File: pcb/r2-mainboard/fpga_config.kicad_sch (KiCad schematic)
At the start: 32 parts, among them U700 XC6SLX-FTG256, U902 W25Q128JVSIQ, X900 33.33MHz

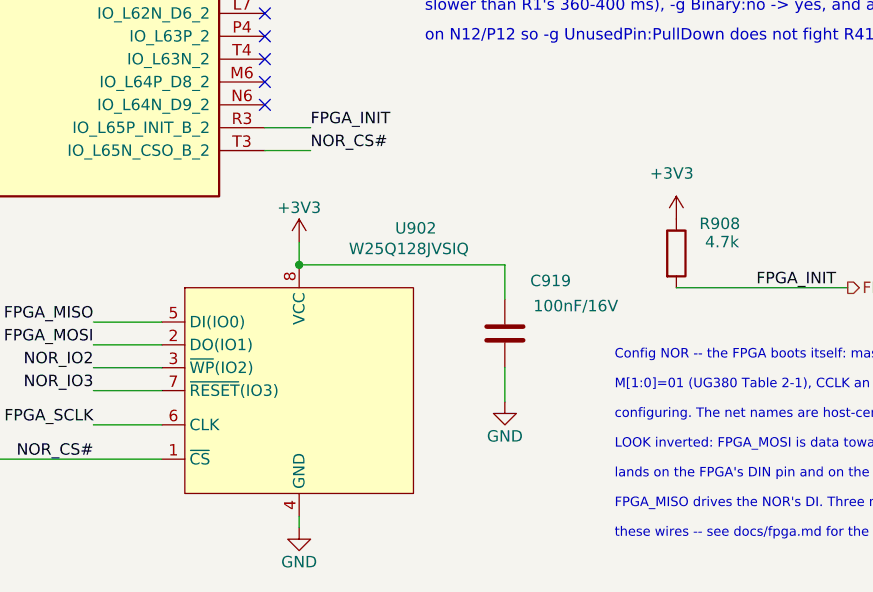
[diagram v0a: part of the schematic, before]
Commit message: changing to osb62x-pm
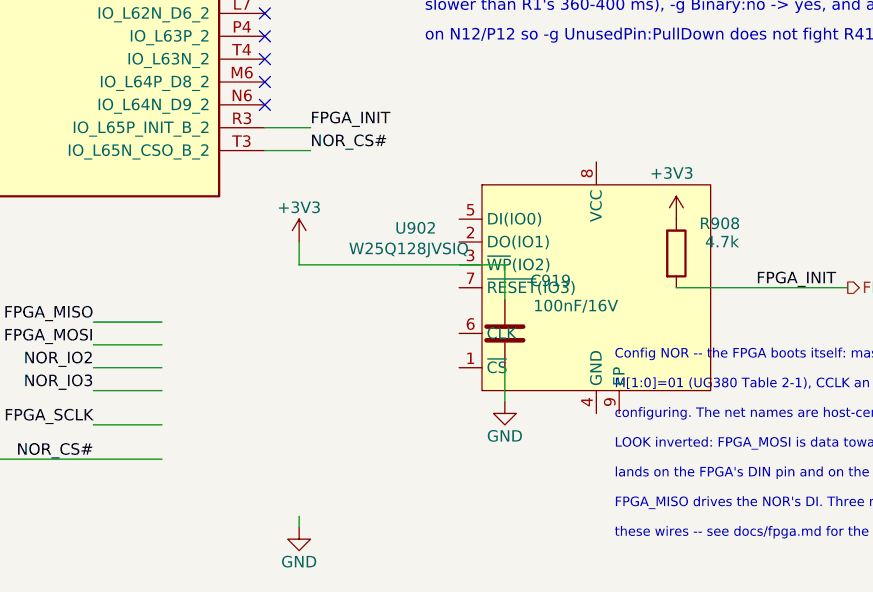
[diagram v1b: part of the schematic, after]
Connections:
- net +3V3: no longer U902.8 (VCC)
- net FPGA_MISO: no longer U902.5 (DI(IO0))
- net FPGA_MOSI: no longer U902.2 (DO(IO1))
- net FPGA_SCLK: no longer U902.6 (CLK)
- net GND: no longer U902.4 (GND)
- net NOR_CS#: no longer U902.1 (~{CS})
- net NOR_IO2: no longer U902.3 (~{WP}(IO2))
- net NOR_IO3: no longer U902.7 (~{RESET}(IO3))
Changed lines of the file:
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@@
 	)
 	(junction
-		(at 87.63 162.56)
-		(diameter 0)
-		(color 0 0 0 0)
-	)
-	(junction
 		(at 175.26 63.5)
 		(diameter 0)
@@
 			)
 		)
-		(property "Description" ""
+		(property "Description" "3.3V CMOS SMD Crystal Clock Oscillator, Abracon"
 			(at 233.68 55.88 0)
 			(hide yes)
@@
 			)
 		)
-		(property "Description" ""
+		(property "Description" "Unpolarized capacitor"
 			(at 208.28 85.09 0)
 			(hide yes)
@@
 			)
 		)
-		(property "Description" ""
+		(property "Description" "Resistor"
 			(at 185.42 35.56 0)
 			(hide yes)
@@
 			)
 		)
-		(property "Description" "NOR supply decoupling"
+		(property "Description" "Unpolarized capacitor"
 			(at 110.49 170.18 0)
 			(hide yes)
@@
 	)
 	(symbol
-		(lib_name "GND_1")
 		(lib_id "power:GND")
 		(at 175.26 71.12 0)
@@
 			)
 		)
-		(property "Description" ""
+		(property "Description" "Unpolarized capacitor"
 			(at 195.58 146.05 0)
 			(hide yes)
@@
 			)
 		)
-		(property "Description" ""
+		(property "Description" "Unpolarized capacitor"
 			(at 208.28 125.73 0)
 			(hide yes)
@@
 			)
 		)
-		(property "Description" ""
+		(property "Description" "Unpolarized capacitor"
 			(at 220.98 146.05 0)
 			(hide yes)
@@
 			)
 		)
-		(property "Description" ""
+		(property "Description" "Unpolarized capacitor"
 			(at 195.58 125.73 0)
 			(hide yes)
@@
 			)
 		)
-		(property "Description" ""
+		(property "Description" "Unpolarized capacitor"
 			(at 208.28 105.41 0)
 			(hide yes)
@@
 	)
 	(symbol
-		(lib_name "GND_1")
 		(lib_id "power:GND")
 		(at 233.68 109.22 0)
@@
 		(pin "8"
 		)
+		(pin "9"
+		)
 		(instances
 			(project "r2"
@@
 			)
 		)
-		(property "Description" ""
+		(property "Description" "Resistor"
 			(at 175.26 35.56 0)
 			(hide yes)
@@
 	)
 	(symbol
-		(lib_name "GND_1")
 		(lib_id "power:GND")
 		(at 233.68 149.86 0)
@@
 			)
 		)
-		(property "Description" ""
+		(property "Description" "Unpolarized capacitor"
 			(at 220.98 85.09 0)
 			(hide yes)
@@
 			)
 		)
-		(property "Description" ""
+		(property "Description" "Unpolarized capacitor"
 			(at 233.68 85.09 0)
 			(hide yes)
@@
 			)
 		)
-		(property "Description" ""
+		(property "Description" "Unpolarized capacitor"
 			(at 195.58 85.09 0)
 			(hide yes)
@@
 			)
 		)
-		(property "Description" ""
+		(property "Description" "Unpolarized capacitor"
 			(at 233.68 105.41 0)
 			(hide yes)
@@
 			)
 		)
-		(property "Description" "Series limit on the SoM's NOR chip select: the FPGA drives CSO_B during configuration, so the two briefly contend if software gets it wrong"
+		(property "Description" "Resistor"
 			(at 36.83 184.15 270)
 			(hide yes)
@@
 			)
 		)
-		(property "Description" ""
+		(property "Description" "Unpolarized capacitor"
 			(at 233.68 146.05 0)
 			(hide yes)
@@
 			)
 		)
-		(property "Description" ""
+		(property "Description" "Unpolarized capacitor"
 			(at 208.28 146.05 0)
 			(hide yes)
@@
 			)
 		)
-		(property "Description" ""
+		(property "Description" "Unpolarized capacitor"
 			(at 220.98 125.73 0)
 			(hide yes)
@@
 			)
 		)
-		(property "Description" ""
+		(property "Description" "Unpolarized capacitor"
 			(at 195.58 105.41 0)
 			(hide yes)
@@
 			)
 		)
-		(property "Description" "UG380 Fig 2-13 note 4: MISO[2]/MISO[3] need pull-ups to VCCO_2."
+		(property "Description" "Resistor"
 			(at 114.3 96.52 0)
 			(hide yes)
@@
 			)
 		)
-		(property "Description" "INIT_B pull-up. R1 leaves this pin floating; with self-boot, INIT_B low is what separates a config error from 'still loading' when DONE never comes"
+		(property "Description" "Resistor"
 			(at 129.54 161.29 0)
 			(hide yes)
@@
 	)
 	(symbol
-		(lib_name "GND_1")
 		(lib_id "power:GND")
 		(at 246.38 129.54 0)
@@
 			)
 		)
-		(property "Description" ""
+		(property "Description" "Unpolarized capacitor"
 			(at 215.9 52.07 0)
 			(hide yes)
@@
 			)
 		)
-		(property "Description" ""
+		(property "Description" "Power symbol creates a global label with name \"+3V3\""
 			(at 96.52 58.42 0)
 			(hide yes)
@@
 			)
 		)
-		(property "Description" "NOR_CS# pull-up -- holds the flash deselected when neither the FPGA nor the SoM drives it"
+		(property "Description" "Resistor"
 			(at 44.45 180.34 0)
 			(hide yes)
@@
 			)
 		)
-		(property "Description" "UG380 Fig 2-13 note 4: MISO[2]/MISO[3] need pull-ups to VCCO_2."
+		(property "Description" "Resistor"
 			(at 139.7 96.52 0)
 			(hide yes)
@@
 			)
 		)
-		(property "Description" ""
+		(property "Description" "Unpolarized capacitor"
 			(at 246.38 125.73 0)
 			(hide yes)
@@
 			)
 		)
-		(property "Description" ""
+		(property "Description" "Resistor"
 			(at 175.26 67.31 0)
 			(hide yes)
@@
 			)
 		)
-		(property "Description" ""
+		(property "Description" "Unpolarized capacitor"
 			(at 246.38 85.09 0)
 			(hide yes)
@@
 	)
 	(symbol
-		(lib_name "GND_1")
 		(lib_id "power:GND")
 		(at 246.38 88.9 0)
@@
 			)
 		)
-		(property "Description" ""
+		(property "Description" "Unpolarized capacitor"
 			(at 220.98 105.41 0)
 			(hide yes)
@@
 			)
 		)
-		(property "Description" ""
+		(property "Description" "Unpolarized capacitor"
 			(at 233.68 125.73 0)
 			(hide yes)
@@
 			)
 		)
-		(property "Description" ""
+		(property "Description" "Power symbol creates a global label with name \"GND\" , ground"
 			(at 87.63 191.77 0)
 			(hide yes)
@@
 			)
 		)
-		(property "Description" ""
+		(property "Description" "Power symbol creates a global label with name \"+3V3\""
 			(at 233.68 142.24 0)
 			(hide yes)
@@
 	)
 	(symbol
-		(lib_name "GND_1")
 		(lib_id "power:GND")
 		(at 233.68 63.5 0)
@@
 			)
 		)
-		(property "Description" ""
+		(property "Description" "Power symbol creates a global label with name \"+3V3\""
 			(at 96.52 76.2 0)
 			(hide yes)
@@
 			)
 		)
-		(property "Description" ""
+		(property "Description" "Power symbol creates a global label with name \"GND\" , ground"
 			(at 110.49 177.8 0)
 			(hide yes)
@@
 			)
 		)
-		(property "Description" ""
+		(property "Description" "Resistor"
 			(at 250.19 55.88 0)
 			(hide yes)

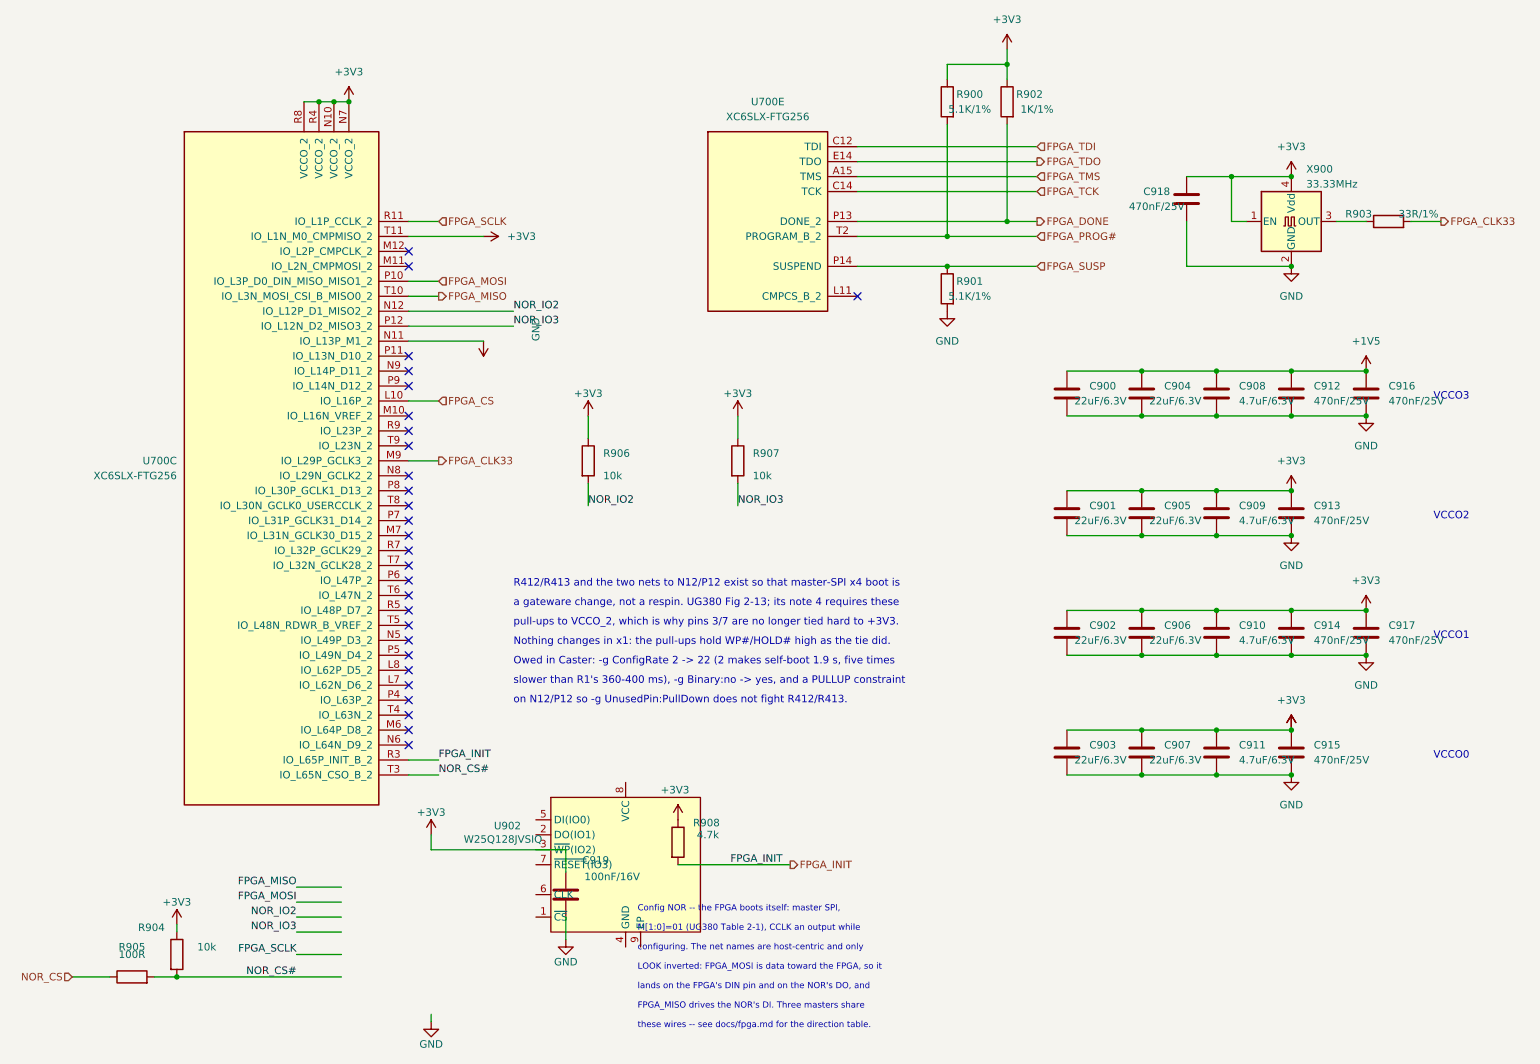
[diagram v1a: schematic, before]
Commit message: Schematics update for new chip.
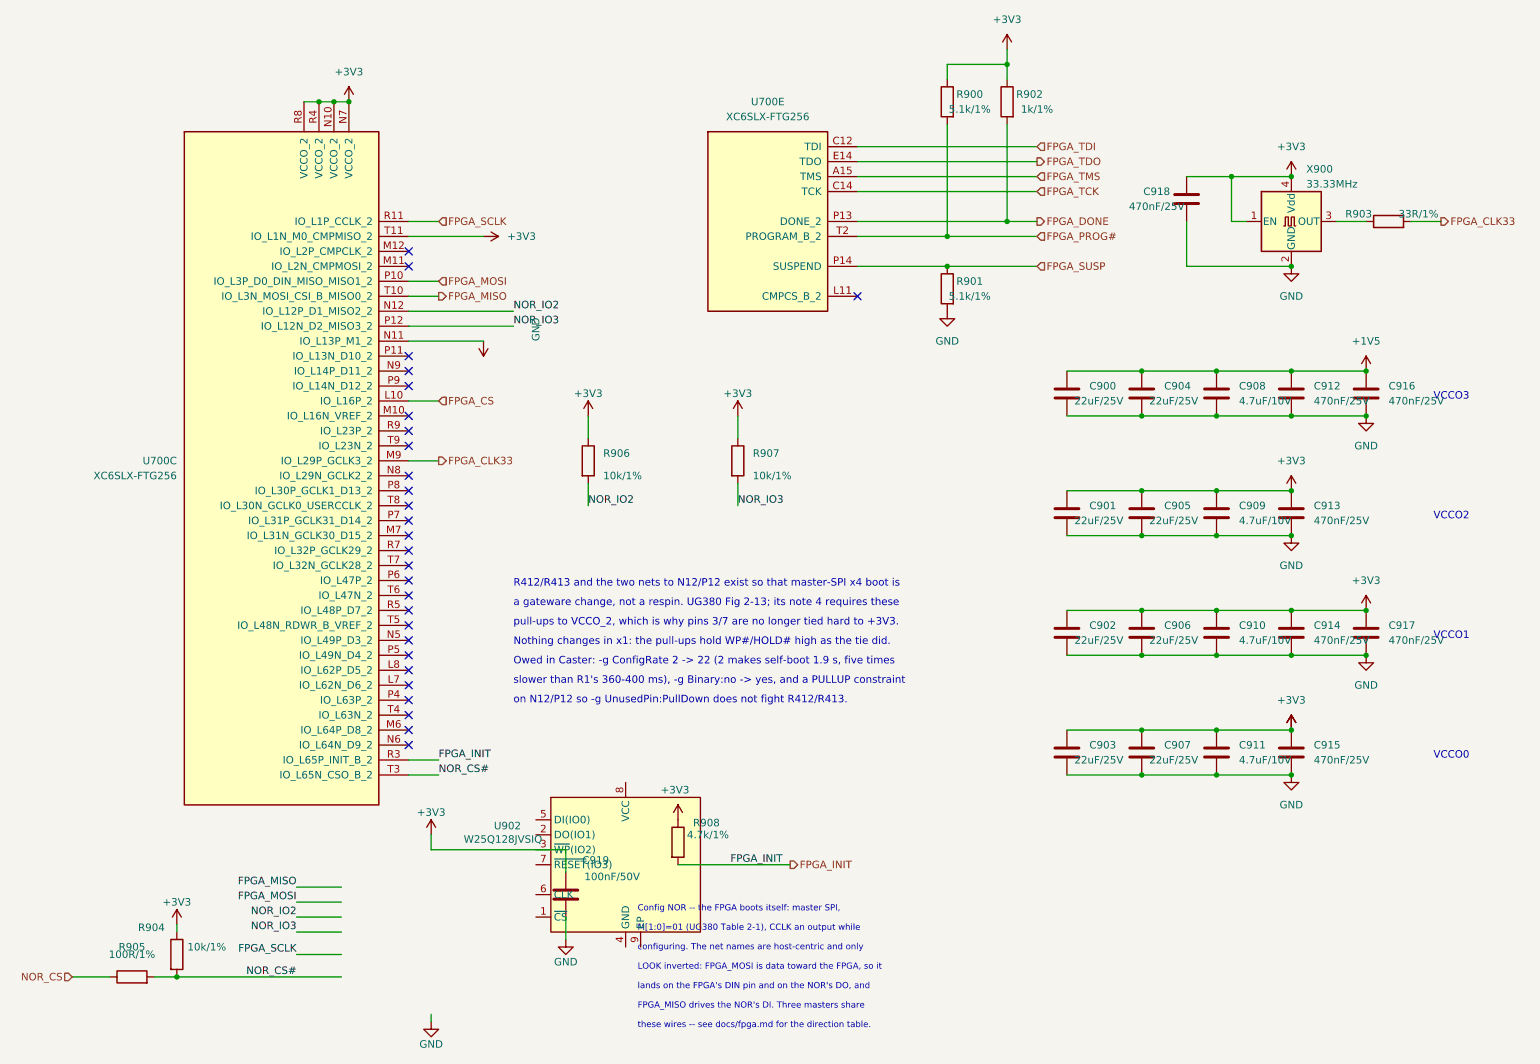
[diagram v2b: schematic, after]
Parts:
- C900, C901, C902, C903, C904, C905, C906, C907: value 22uF/6.3V -> 22uF/25V; footprint Capacitor_SMD:C_0603_1608Metric -> Capacitor_SMD:C_0805_2012Metric
- C908, C909, C910, C911: value 4.7uF/6.3V -> 4.7uF/10V
- C919: value 100nF/16V -> 100nF/50V
- R900, R901: value 5.1K/1% -> 5.1k/1%
- R902: value 1K/1% -> 1k/1%
- R904, R906, R907: value 10k -> 10k/1%
- R905: value 100R -> 100R/1%
- R908: value 4.7k -> 4.7k/1%
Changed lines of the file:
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@@
 			)
 		)
-		(property "Value" "22uF/6.3V"
+		(property "Value" "22uF/25V"
 			(at 209.55 86.36 0)
 			(show_name no)
@@
 			)
 		)
-		(property "Footprint" "Capacitor_SMD:C_0603_1608Metric"
+		(property "Footprint" "Capacitor_SMD:C_0805_2012Metric"
 			(at 209.2452 88.9 0)
 			(hide yes)
@@
 			)
 		)
-		(property "Value" "1K/1%"
+		(property "Value" "1k/1%"
 			(at 190.5 36.83 0)
 			(show_name no)
@@
 			)
 		)
-		(property "Value" "100nF/16V"
+		(property "Value" "100nF/50V"
 			(at 118.364 167.132 0)
 			(show_name no)
@@
 			)
 		)
-		(property "Value" "22uF/6.3V"
+		(property "Value" "22uF/25V"
 			(at 196.85 147.32 0)
 			(show_name no)
@@
 			)
 		)
-		(property "Footprint" "Capacitor_SMD:C_0603_1608Metric"
+		(property "Footprint" "Capacitor_SMD:C_0805_2012Metric"
 			(at 196.5452 149.86 0)
 			(hide yes)
@@
 			)
 		)
-		(property "Value" "22uF/6.3V"
+		(property "Value" "22uF/25V"
 			(at 209.55 127 0)
 			(show_name no)
@@
 			)
 		)
-		(property "Footprint" "Capacitor_SMD:C_0603_1608Metric"
+		(property "Footprint" "Capacitor_SMD:C_0805_2012Metric"
 			(at 209.2452 129.54 0)
 			(hide yes)
@@
 			)
 		)
-		(property "Value" "4.7uF/6.3V"
+		(property "Value" "4.7uF/10V"
 			(at 224.79 147.32 0)
 			(show_name no)
@@
 			)
 		)
-		(property "Value" "22uF/6.3V"
+		(property "Value" "22uF/25V"
 			(at 196.85 127 0)
 			(show_name no)
@@
 			)
 		)
-		(property "Footprint" "Capacitor_SMD:C_0603_1608Metric"
+		(property "Footprint" "Capacitor_SMD:C_0805_2012Metric"
 			(at 196.5452 129.54 0)
 			(hide yes)
@@
 			)
 		)
-		(property "Value" "22uF/6.3V"
+		(property "Value" "22uF/25V"
 			(at 209.55 106.68 0)
 			(show_name no)
@@
 			)
 		)
-		(property "Footprint" "Capacitor_SMD:C_0603_1608Metric"
+		(property "Footprint" "Capacitor_SMD:C_0805_2012Metric"
 			(at 209.2452 109.22 0)
 			(hide yes)
@@
 			)
 		)
-		(property "Value" "5.1K/1%"
+		(property "Value" "5.1k/1%"
 			(at 179.07 36.83 0)
 			(show_name no)
@@
 			)
 		)
-		(property "Value" "4.7uF/6.3V"
+		(property "Value" "4.7uF/10V"
 			(at 224.79 86.36 0)
 			(show_name no)
@@
 			)
 		)
-		(property "Value" "22uF/6.3V"
+		(property "Value" "22uF/25V"
 			(at 196.85 86.36 0)
 			(show_name no)
@@
 			)
 		)
-		(property "Footprint" "Capacitor_SMD:C_0603_1608Metric"
+		(property "Footprint" "Capacitor_SMD:C_0805_2012Metric"
 			(at 196.5452 88.9 0)
 			(hide yes)
@@
 			)
 		)
-		(property "Value" "100R"
+		(property "Value" "100R/1%"
 			(at 36.83 180.34 270)
 			(show_name no)
@@
 			)
 		)
-		(property "Value" "22uF/6.3V"
+		(property "Value" "22uF/25V"
 			(at 209.55 147.32 0)
 			(show_name no)
@@
 			)
 		)
-		(property "Footprint" "Capacitor_SMD:C_0603_1608Metric"
+		(property "Footprint" "Capacitor_SMD:C_0805_2012Metric"
 			(at 209.2452 149.86 0)
 			(hide yes)
@@
 			)
 		)
-		(property "Value" "4.7uF/6.3V"
+		(property "Value" "4.7uF/10V"
 			(at 224.79 127 0)
 			(show_name no)
@@
 			)
 		)
-		(property "Value" "22uF/6.3V"
+		(property "Value" "22uF/25V"
 			(at 196.85 106.68 0)
 			(show_name no)
@@
 			)
 		)
-		(property "Footprint" "Capacitor_SMD:C_0603_1608Metric"
+		(property "Footprint" "Capacitor_SMD:C_0805_2012Metric"
 			(at 196.5452 109.22 0)
 			(hide yes)
@@
 			)
 		)
-		(property "Value" "10k"
+		(property "Value" "10k/1%"
 			(at 116.84 99.06 0)
 			(show_name no)
@@
 			)
 		)
-		(property "Value" "4.7k"
+		(property "Value" "4.7k/1%"
 			(at 134.62 160.02 0)
 			(show_name no)
@@
 			)
 		)
-		(property "Value" "10k"
+		(property "Value" "10k/1%"
 			(at 49.53 179.07 0)
 			(show_name no)
@@
 			)
 		)
-		(property "Value" "10k"
+		(property "Value" "10k/1%"
 			(at 142.24 99.06 0)
 			(show_name no)
@@
 			)
 		)
-		(property "Value" "5.1K/1%"
+		(property "Value" "5.1k/1%"
 			(at 179.07 68.58 0)
 			(show_name no)
@@
 			)
 		)
-		(property "Value" "4.7uF/6.3V"
+		(property "Value" "4.7uF/10V"
 			(at 224.79 106.68 0)
 			(show_name no)
